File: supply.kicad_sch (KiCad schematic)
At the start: 98 parts, among them IC12 74HC00PW, IC13 SN74LVC1G126DCKR, IC4 TPS7A0518PDBVT, J12 533980471, T3 BSS138APW, U1 LM3671MF-3.3/NOPB, U2 LM62440-Q1, U3 SN74LXC1T45DBVR, U5 LM3671MF-3.3/NOPB, U6 SIC477ED-T1-GE3

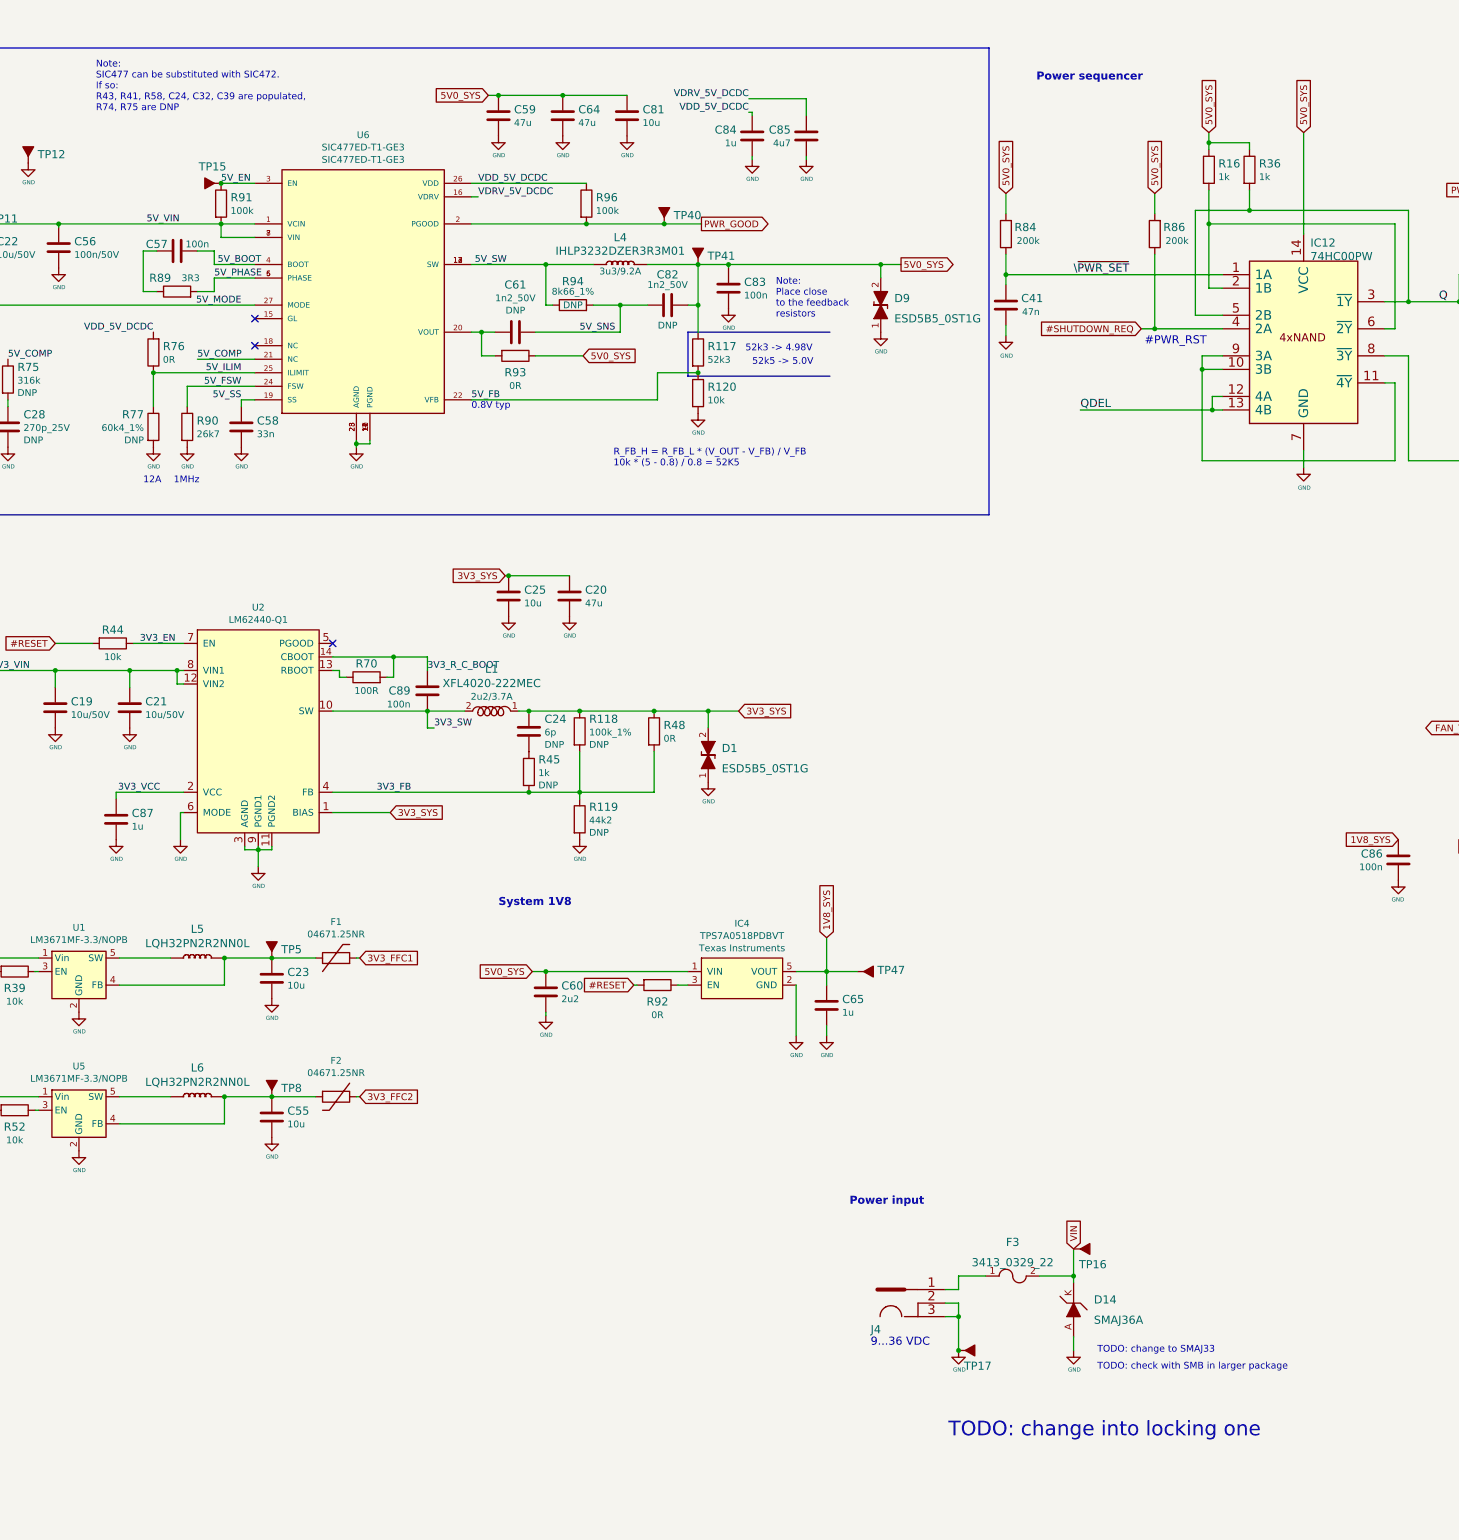
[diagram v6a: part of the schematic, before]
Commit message: Fix SIC477ED note
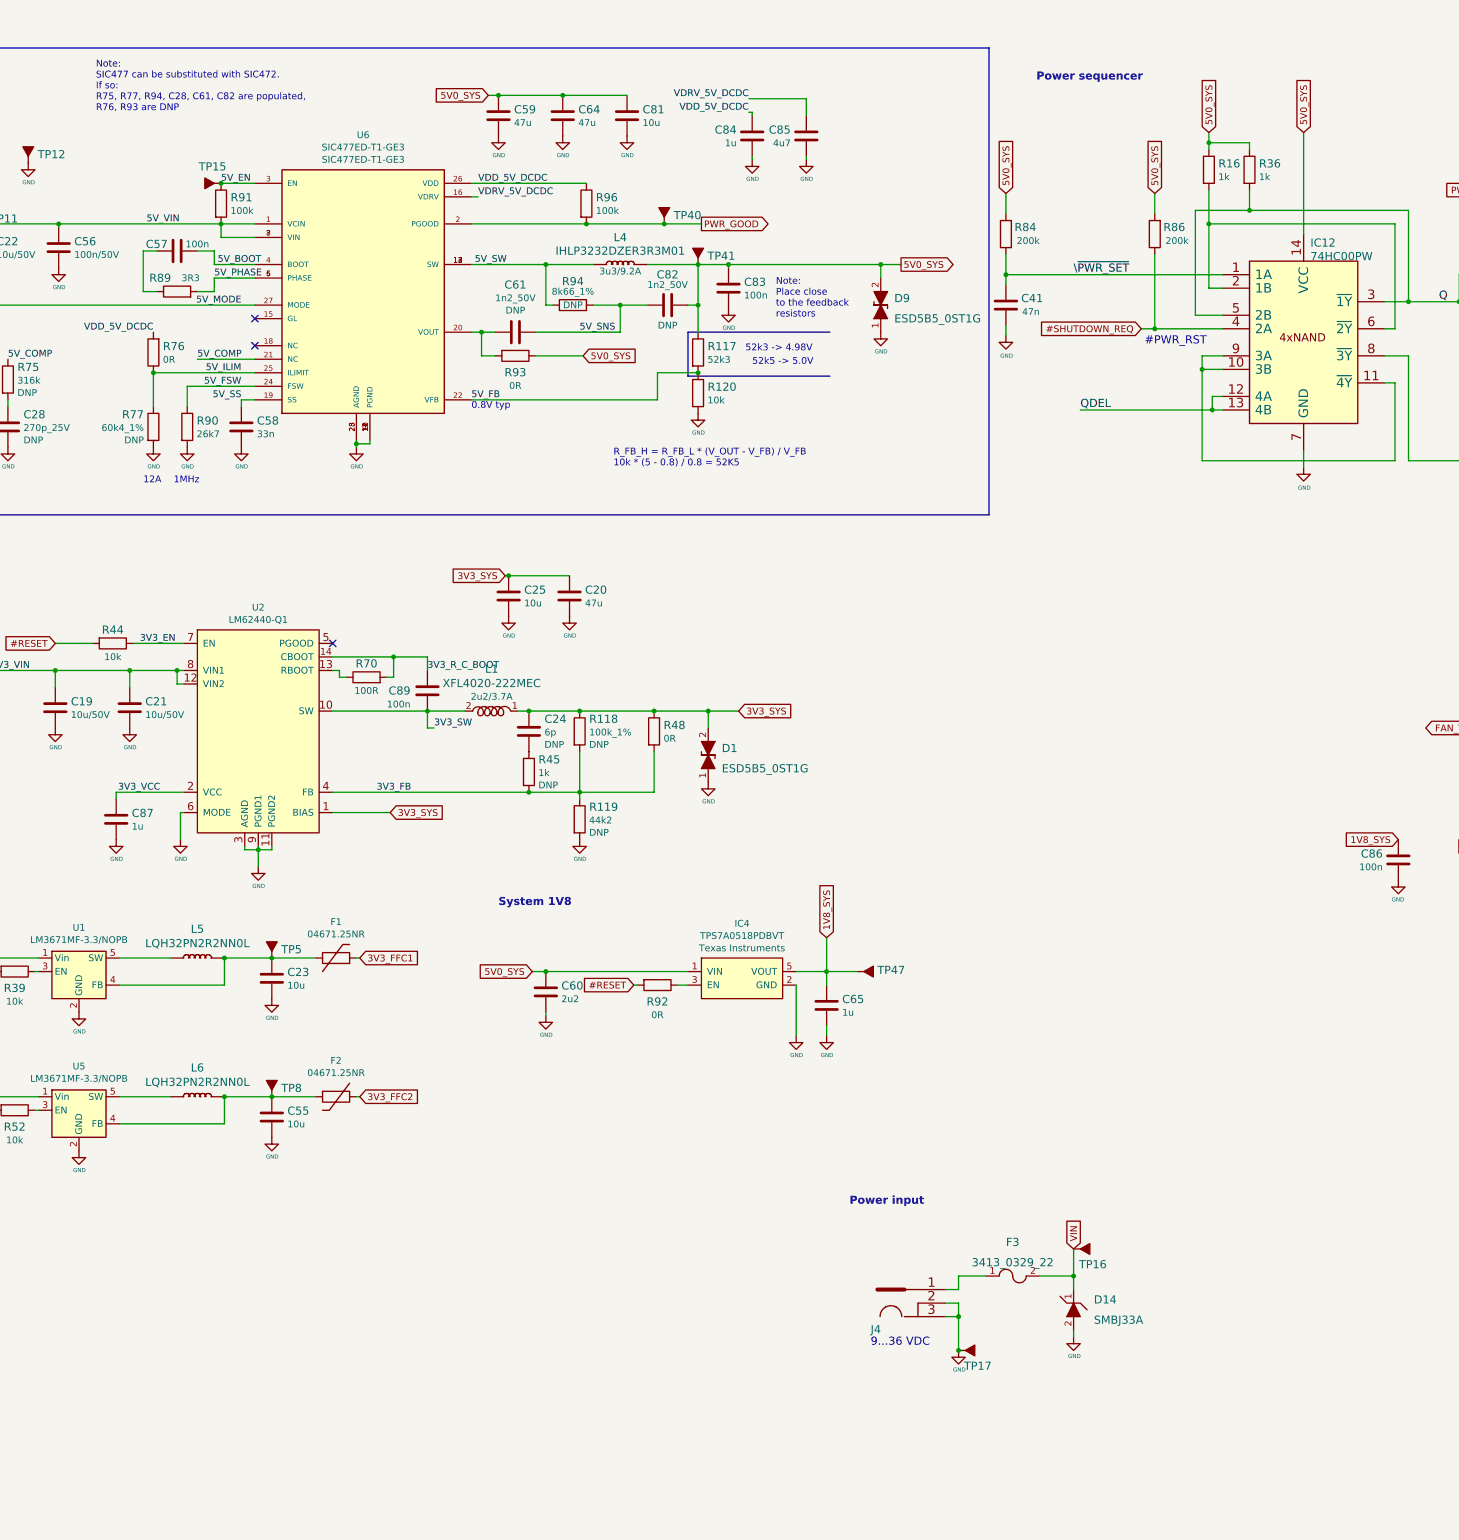
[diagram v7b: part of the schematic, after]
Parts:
- removed D14: SMAJ36A, jetson-nano-baseboard-footprints:DO-214AC, symbol jetson-nano-baseboard:SMAJ36A
- added D14: SMBJ33A, antmicro-footprints:D_SMB, symbol antmicroTVSDiodes:SMBJ33A
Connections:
- net GND: now also D14.2
- net VIN: now also D14.1
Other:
- note added: "Note: SIC477 can be substituted with SIC472. If so: R75, R77, R94, C28, C61, C82 are populated, R76, R93 are DNP"
- note removed: "Note: SIC477 can be substituted with SIC472. If so: R43, R41, R58, C24, C32, C39 are populated, R74, R75 are DNP"
- note removed: "TODO: change into locking one"
- note removed: "TODO: change to SMAJ33"
- note removed: "TODO: check with SMB in larger package"
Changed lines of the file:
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@@
     (stroke (width 0) (type default) (color 0 0 0 0))
   )
-  (wire (pts (xy 252.73 261.62) (xy 252.73 264.16))
+  (wire (pts (xy 252.73 260.35) (xy 252.73 261.62))
     (stroke (width 0) (type default) (color 0 0 0 0))
   )
@@
     (stroke (width 0) (type default) (color 0 0 0 0))
   )
-  (wire (pts (xy 252.73 250.19) (xy 252.73 251.46))
+  (wire (pts (xy 252.73 250.19) (xy 252.73 252.73))
     (stroke (width 0) (type default) (color 0 0 0 0))
   )
@@
     (effects (font (size 2.9972 2.9972) (thickness 0.5994) bold) (justify left bottom))
   )
-  (text "Note:\nSIC477 can be substituted with SIC472.\nIf so:\nR43, R41, R58, C24, C32, C39 are populated,\nR74, R75 are DNP"
+  (text "Note:\nSIC477 can be substituted with SIC472.\nIf so:\nR75, R77, R94, C28, C61, C82 are populated,\nR76, R93 are DNP"
     (at 69.215 31.75 0)
     (effects (font (size 1.27 1.27)) (justify left bottom))
@@
     (effects (font (size 1.27 1.27)) (justify left bottom))
   )
-  (text "TODO: check with SMB in larger package" (at 257.175 267.97 0)
-    (effects (font (size 1.27 1.27)) (justify left bottom))
-  )
   (text "3V3/3.5A\n" (at 22.86 120.65 0)
     (effects (font (size 1.4986 1.4986) (thickness 0.2997) bold) (justify left bottom))
@@
     (effects (font (size 1.4986 1.4986) (thickness 0.2997) bold) (justify left bottom))
   )
-  (text "TODO: change into locking one" (at 229.235 280.67 0)
-    (effects (font (size 2.7432 2.7432)) (justify left bottom))
-  )
   (text "Power save mode enabled, \nVDD, VDRVPre-reg on" (at 40.005 98.425 90)
     (effects (font (size 1.27 1.27)) (justify left bottom))
@@
     (effects (font (size 1.4986 1.4986) (thickness 0.2997) bold) (justify left bottom))
   )
-  (text "TODO: change to SMAJ33" (at 257.175 264.795 0)
-    (effects (font (size 1.27 1.27)) (justify left bottom))
-  )
   (text "System 1V8" (at 144.78 180.975 0)
     (effects (font (size 1.4986 1.4986) (thickness 0.2997) bold) (justify left bottom))
@@
     (pin "2")
   )
-  (symbol (lib_id "jetson-nano-baseboard:SMAJ36A") (at 252.73 256.54 90) (unit 1)
+  (symbol (lib_id "antmicroTVSDiodes:SMBJ33A") (at 252.73 256.54 90) (unit 1)
     (in_bom yes) (on_board yes) (fields_autoplaced)
     (property "Reference" "D14" (id 0) (at 256.54 254.635 90)
       (effects (font (size 1.524 1.524)) (justify right))
     )
-    (property "Value" "SMAJ36A" (id 1) (at 256.54 258.445 90)
+    (property "Value" "SMBJ33A" (id 1) (at 256.54 258.445 90)
       (effects (font (size 1.524 1.524)) (justify right))
     )
-    (property "Footprint" "jetson-nano-baseboard-footprints:DO-214AC" (id 2) (at 247.65 251.46 0)
+    (property "Footprint" "antmicro-footprints:D_SMB" (id 2) (at 247.65 251.46 0)
       (effects (font (size 1.524 1.524)) (justify left) hide)
     )
-    (property "Datasheet" "https://www.mouser.pl/datasheet/2/447/SMAJ_1-1954892.pdf" (id 3) (at 245.11 251.46 0)
+    (property "Datasheet" "https://www.mouser.pl/datasheet/2/408/DF2S30FS_datasheet_en_20211216-1916197.pdf" (id 3) (at 245.11 251.46 0)
       (effects (font (size 1.524 1.524)) (justify left) hide)
     )
-    (property "Manufacturer" "YAGEO" (id 4) (at 237.49 251.46 0)
+    (property "Manufacturer" "Littelfuse" (id 4) (at 224.79 251.46 0)
       (effects (font (size 1.524 1.524)) (justify left) hide)
     )
-    (property "MPN" "SMAJ36A/TR13" (id 5) (at 240.03 251.46 0)
+    (property "MPN" "SMBJ33A" (id 5) (at 240.03 251.46 0)
       (effects (font (size 1.524 1.524)) (justify left) hide)
     )
-    (pin "A")
-    (pin "K")
+    (pin "1")
+    (pin "2")
   )
   (symbol (lib_id "jetson-nano-baseboard:ESD5B5_0ST1G") (at 216.535 67.945 90) (unit 1)
@@
     (pin "2")
   )
-  (symbol (lib_id "jetson-nano-baseboard:GND") (at 252.73 264.16 0) (unit 1)
+  (symbol (lib_id "jetson-nano-baseboard:GND") (at 252.73 261.62 0) (unit 1)
     (in_bom yes) (on_board yes)
-    (property "Reference" "#GND_0116" (id 0) (at 252.73 264.16 0)
+    (property "Reference" "#GND_0116" (id 0) (at 252.73 261.62 0)
       (effects (font (size 0.508 0.508)) hide)
     )
-    (property "Value" "GND" (id 1) (at 252.8824 267.7668 0)
+    (property "Value" "GND" (id 1) (at 252.8824 265.2268 0)
       (effects (font (size 0.762 0.762)))
     )
-    (property "Footprint" "" (id 2) (at 252.73 264.16 0)
+    (property "Footprint" "" (id 2) (at 252.73 261.62 0)
       (effects (font (size 1.778 1.778)) hide)
     )
-    (property "Datasheet" "" (id 3) (at 252.73 264.16 0)
+    (property "Datasheet" "" (id 3) (at 252.73 261.62 0)
       (effects (font (size 1.778 1.778)) hide)
     )

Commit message: Update local libraries
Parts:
- D14: footprint antmicro-footprints:D_SMB -> jetson-nano-baseboard-footprints:D_SMB; symbol antmicroTVSDiodes:SMBJ33A -> jetson-nano-baseboard:SMBJ33A
